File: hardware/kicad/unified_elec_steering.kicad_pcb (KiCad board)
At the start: 2 copper layers, 99 x 99 mm, 23 parts, among them J10 Conn_01x03, J11 Conn_01x03, J12 Conn_01x04, J13 Conn_01x03, J3 Conn_01x02, J4 Conn_01x03, J5 Conn_01x03, J6 Conn_01x04, J7 Conn_01x06, J8 Conn_01x06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

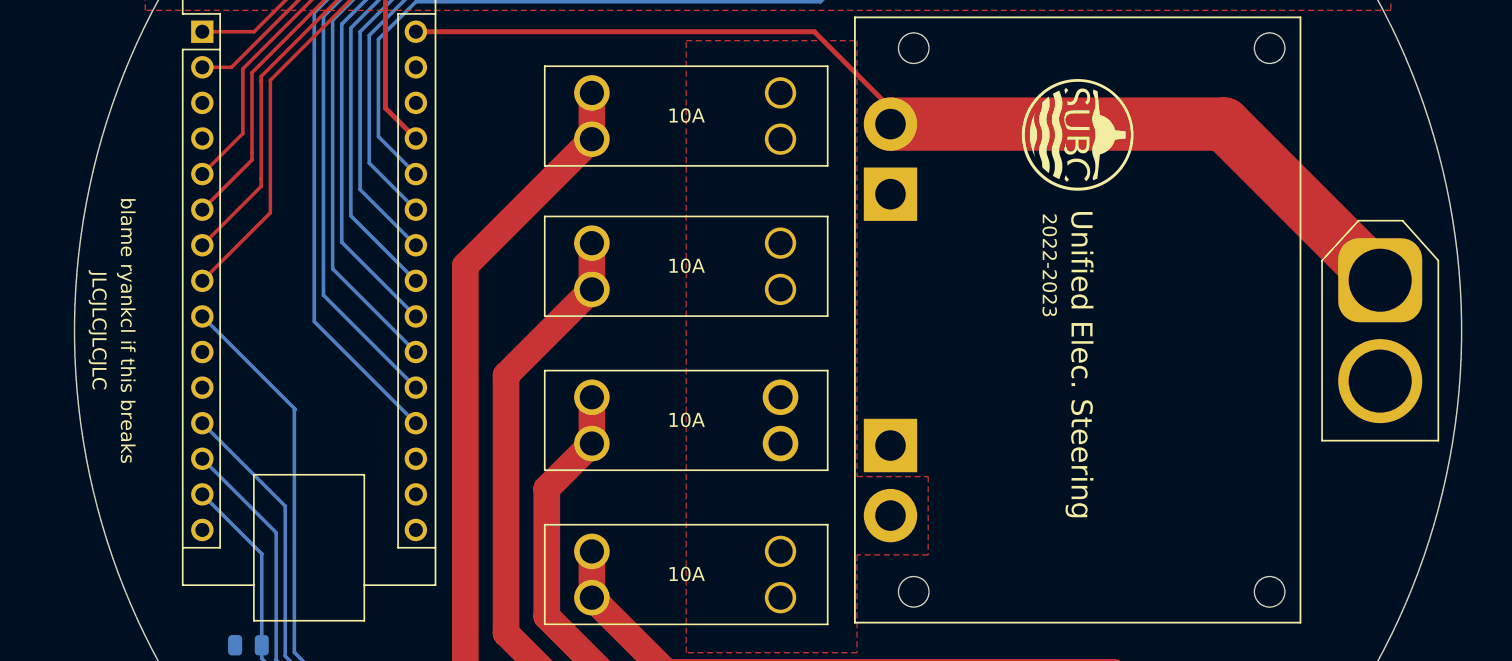
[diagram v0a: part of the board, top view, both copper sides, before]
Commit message: add mounting holes
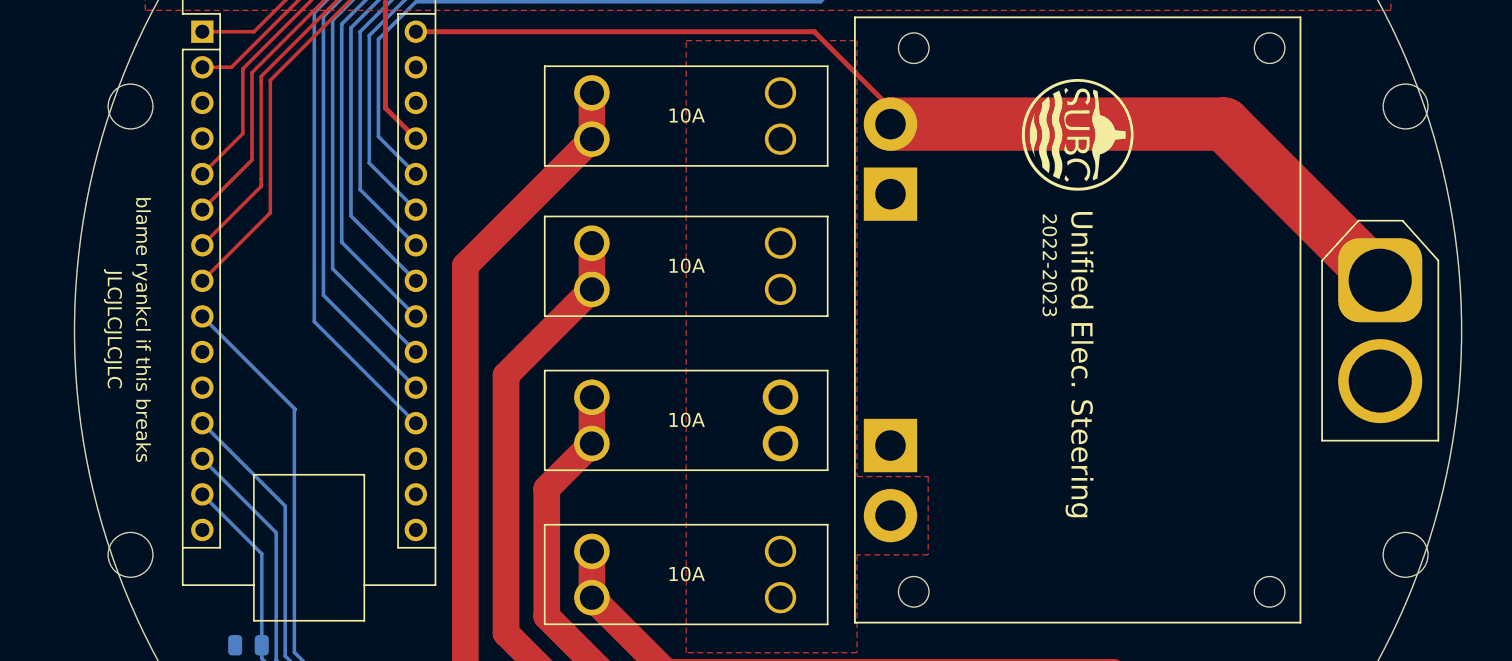
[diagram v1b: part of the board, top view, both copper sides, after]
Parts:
- added REF**: MountingHole_3.2mm_M3, MountingHole:MountingHole_3.2mm_M3, F.Cu at (-45.5, 16.0)
- added REF**: MountingHole_3.2mm_M3, MountingHole:MountingHole_3.2mm_M3, F.Cu at (-45.5, -16.0)
- added REF**: MountingHole_3.2mm_M3, MountingHole:MountingHole_3.2mm_M3, F.Cu at (45.5, -16.0)
- added REF**: MountingHole_3.2mm_M3, MountingHole:MountingHole_3.2mm_M3, F.Cu at (45.5, 16.0)
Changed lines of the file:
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@@
       (disableapertmacros false)
       (usegerberextensions true)
-      (usegerberattributes true)
-      (usegerberadvancedattributes true)
-      (creategerberjobfile true)
+      (usegerberattributes false)
+      (usegerberadvancedattributes false)
+      (creategerberjobfile false)
       (svguseinch false)
       (svgprecision 6)
@@
       (psa4output false)
       (plotreference true)
-      (plotvalue true)
+      (plotvalue false)
       (plotinvisibletext false)
       (sketchpadsonfab false)
@@
     )
   )
+  (footprint "MountingHole:MountingHole_3.2mm_M3" (layer "F.Cu")
+    (at -45.5 16)
+    (descr "Mounting Hole 3.2mm, no annular, M3")
+    (tags "mounting hole 3.2mm no annular m3")
+    (attr exclude_from_pos_files exclude_from_bom)
+    (fp_text reference "REF**" (at 0 -4.2) (layer "F.SilkS") hide
+      (effects (font (size 1 1) (thickness 0.15)))
+    )
+    (fp_text value "MountingHole_3.2mm_M3" (at 0 4.2) (layer "F.Fab")
+      (effects (font (size 1 1) (thickness 0.15)))
+    )
+    (fp_text user "${REFERENCE}" (at 0 0) (layer "F.Fab")
+      (effects (font (size 1 1) (thickness 0.15)))
+    )
+    (fp_circle (center 0 0) (end 3.2 0) (layer "Cmts.User") (width 0.15) (fill none))
+    (fp_circle (center 0 0) (end 3.45 0) (layer "F.CrtYd") (width 0.05) (fill none))
+    (pad "" np_thru_hole circle (at 0 0) (size 3.2 3.2) (drill 3.2) (layers F&B.Cu *.Mask))
+  )
   (footprint "LOGO" (layer "F.Cu")
     (at 22.098204 -13.974236 -90)
@@
     )
   )
+  (footprint "MountingHole:MountingHole_3.2mm_M3" (layer "F.Cu")
+    (at -45.5 -16)
+    (descr "Mounting Hole 3.2mm, no annular, M3")
+    (tags "mounting hole 3.2mm no annular m3")
+    (attr exclude_from_pos_files exclude_from_bom)
+    (fp_text reference "REF**" (at 0 -4.2) (layer "F.SilkS") hide
+      (effects (font (size 1 1) (thickness 0.15)))
+    )
+    (fp_text value "MountingHole_3.2mm_M3" (at 0 4.2) (layer "F.Fab")
+      (effects (font (size 1 1) (thickness 0.15)))
+    )
+    (fp_text user "${REFERENCE}" (at 0 0) (layer "F.Fab")
+      (effects (font (size 1 1) (thickness 0.15)))
+    )
+    (fp_circle (center 0 0) (end 3.2 0) (layer "Cmts.User") (width 0.15) (fill none))
+    (fp_circle (center 0 0) (end 3.45 0) (layer "F.CrtYd") (width 0.05) (fill none))
+    (pad "" np_thru_hole circle (at 0 0) (size 3.2 3.2) (drill 3.2) (layers *.Cu *.Mask))
+  )
   (footprint "elec_steering:3557-2" (layer "F.Cu")
     (at -5.842 -6.246)
@@
     )
   )
+  (footprint "MountingHole:MountingHole_3.2mm_M3" (layer "F.Cu")
+    (at 45.5 -16)
+    (descr "Mounting Hole 3.2mm, no annular, M3")
+    (tags "mounting hole 3.2mm no annular m3")
+    (attr exclude_from_pos_files exclude_from_bom)
+    (fp_text reference "REF**" (at 0 -4.2) (layer "F.SilkS") hide
+      (effects (font (size 1 1) (thickness 0.15)))
+    )
+    (fp_text value "MountingHole_3.2mm_M3" (at 0 4.2) (layer "F.Fab")
+      (effects (font (size 1 1) (thickness 0.15)))
+    )
+    (fp_text user "${REFERENCE}" (at 0 0) (layer "F.Fab")
+      (effects (font (size 1 1) (thickness 0.15)))
+    )
+    (fp_circle (center 0 0) (end 3.2 0) (layer "Cmts.User") (width 0.15) (fill none))
+    (fp_circle (center 0 0) (end 3.45 0) (layer "F.CrtYd") (width 0.05) (fill none))
+    (pad "" np_thru_hole circle (at 0 0) (size 3.2 3.2) (drill 3.2) (layers *.Cu *.Mask))
+  )
   (footprint "elec_steering:1722861103" (layer "F.Cu")
     (at 24.474832 34.126705 40)
@@
     )
   )
+  (footprint "MountingHole:MountingHole_3.2mm_M3" (layer "F.Cu")
+    (at 45.5 16)
+    (descr "Mounting Hole 3.2mm, no annular, M3")
+    (tags "mounting hole 3.2mm no annular m3")
+    (attr exclude_from_pos_files exclude_from_bom)
+    (fp_text reference "REF**" (at 0 -4.2) (layer "F.SilkS") hide
+      (effects (font (size 1 1) (thickness 0.15)))
+    )
+    (fp_text value "MountingHole_3.2mm_M3" (at 0 4.2) (layer "F.Fab")
+      (effects (font (size 1 1) (thickness 0.15)))
+    )
+    (fp_text user "${REFERENCE}" (at 0 0) (layer "F.Fab")
+      (effects (font (size 1 1) (thickness 0.15)))
+    )
+    (fp_circle (center 0 0) (end 3.2 0) (layer "Cmts.User") (width 0.15) (fill none))
+    (fp_circle (center 0 0) (end 3.45 0) (layer "F.CrtYd") (width 0.05) (fill none))
+    (pad "" np_thru_hole circle (at 0 0) (size 3.2 3.2) (drill 3.2) (layers *.Cu *.Mask))
+  )
   (footprint "Connector_Molex:Molex_SL_171971-0006_1x06_P2.54mm_Vertical" (layer "F.Cu")
     (at -3.65 -31 180)
@@
     (effects (font (size 1 1) (thickness 0.15)) (justify left))
   )
-  (gr_text "JLCJLCJLCJLC" (at -47.752 0 270) (layer "F.SilkS")
+  (gr_text "JLCJLCJLCJLC" (at -46.6598 -0.0762 270) (layer "F.SilkS")
     (effects (font (size 1 1) (thickness 0.15)))
   )
@@
     (effects (font (size 1 1) (thickness 0.15)))
   )
-  (gr_text "blame ryankcl if this breaks" (at -45.72 0 270) (layer "F.SilkS")
+  (gr_text "blame ryankcl if this breaks" (at -44.6278 -0.0762 270) (layer "F.SilkS")
     (effects (font (size 1 1) (thickness 0.15)))
   )
